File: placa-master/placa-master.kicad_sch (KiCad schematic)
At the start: 3 parts, among them J10 Enlace_placas, U4 MCP23017-E/SO

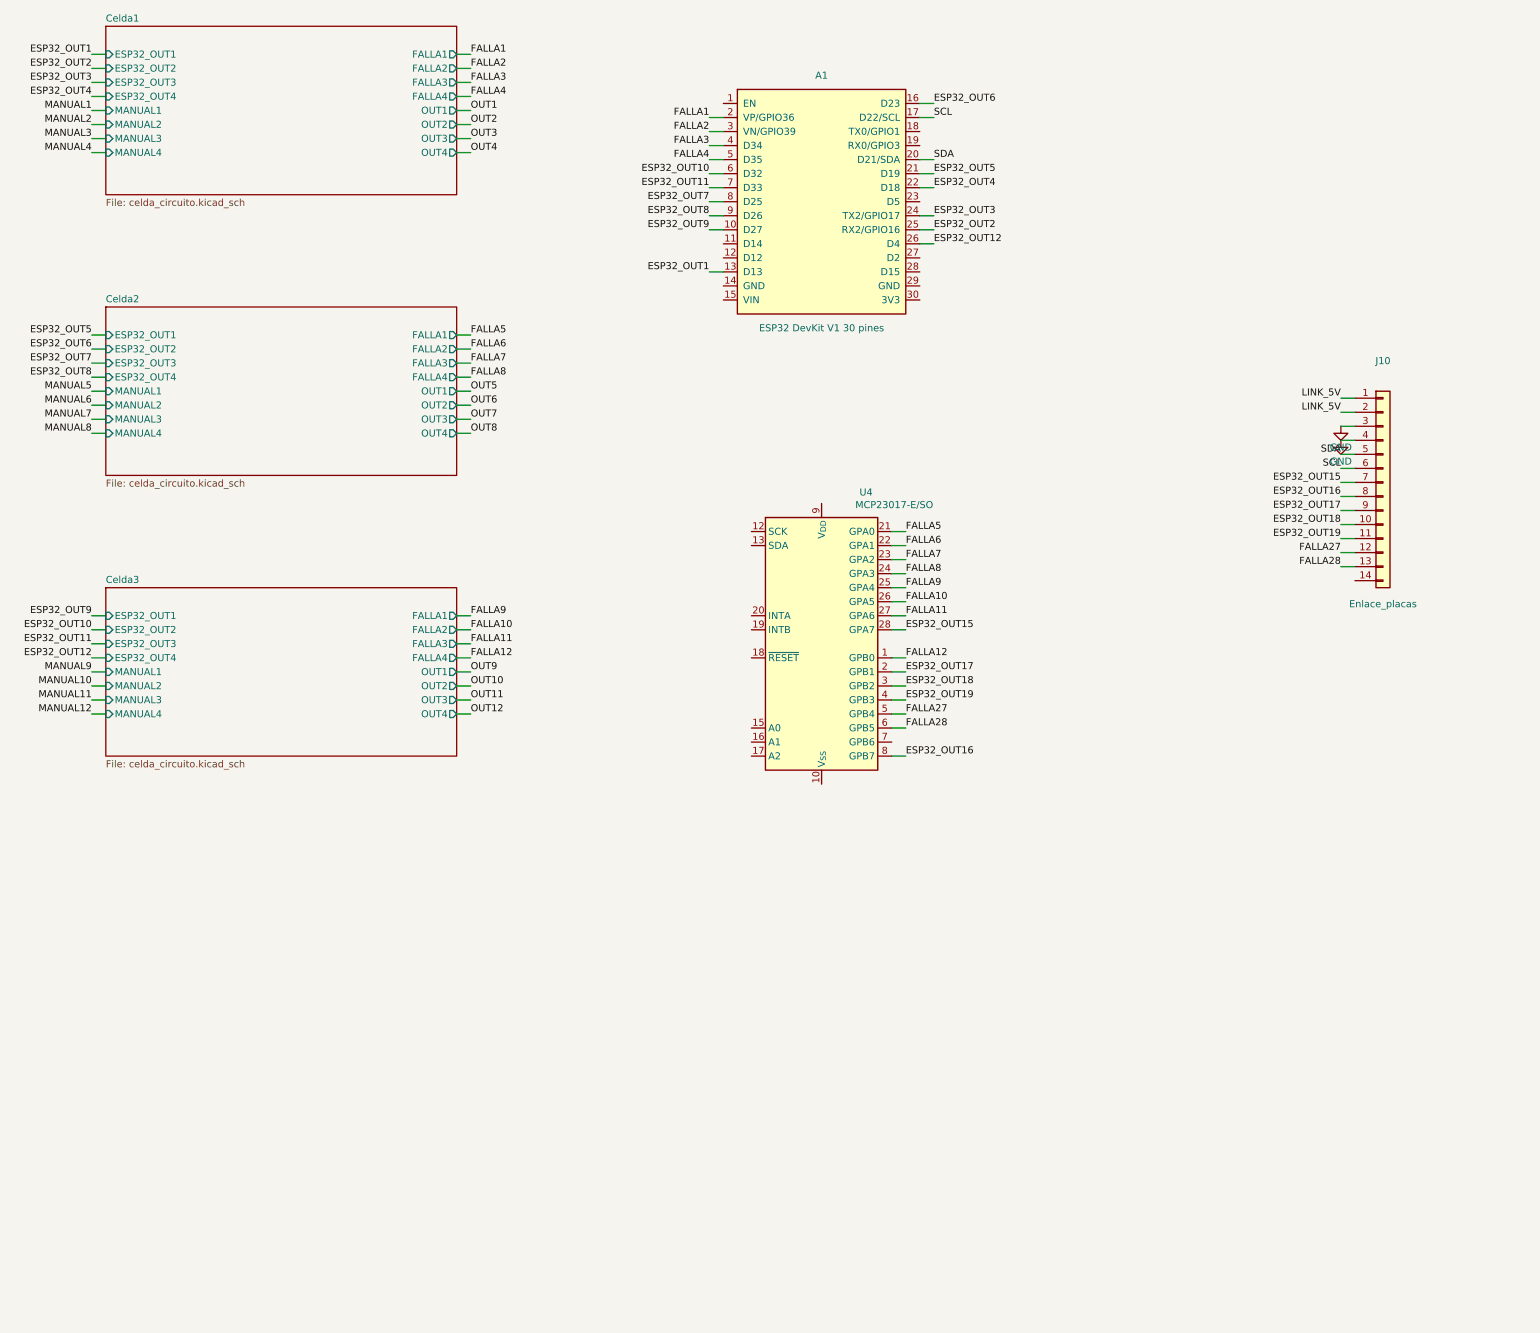
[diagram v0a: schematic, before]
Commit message: Cablea alimentación e I2C de las placas y replica las celdas en los PCB
Esquemáticos raíz: se cablean VDD, VSS, RESET, direcciones y SDA/SCL de los
MCP, los pull-ups de I2C (solo en la master), el LDO de 3,3 V y la entrada de
+12 V de la master, y la unión de las redes del bloque de poder en la slave.

PCB: nuevo herramientas/replicar_celdas_pcb.py que copia la celda dorada por
traslación en cada placa (master en una fila de 3 celdas, slave en 2 x 2), con
pistas, vías, serigrafía y planos GND/+3,3 V. Coloca además las huellas de la
raíz (ESP32, MCP, bloque de poder, conector) en una franja provisional bajo
las celdas, ya enlazadas al esquemático. Sin tiras de +12 V a propósito: se
dibujan al final. La master incluye los ajustes manuales hechos en KiCad.
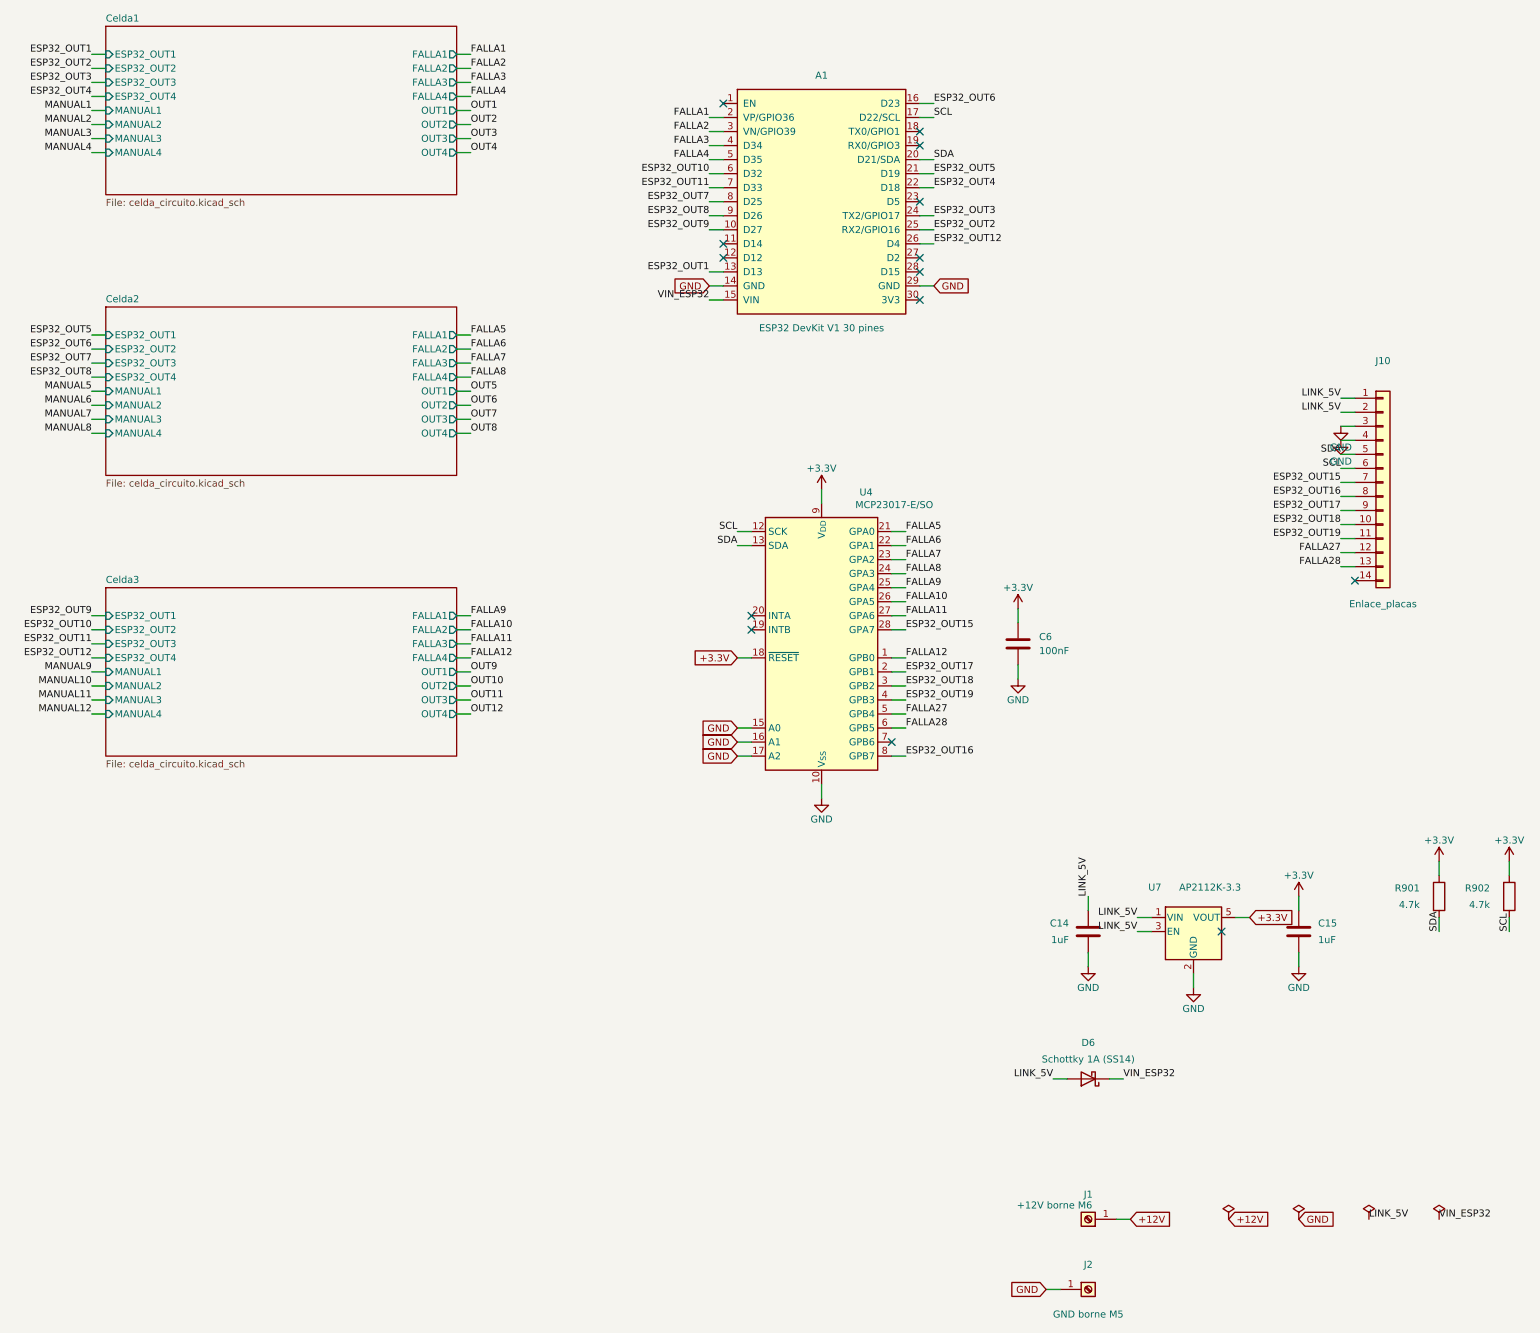
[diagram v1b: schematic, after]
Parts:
- added C14, C15: 1uF, Capacitor_SMD:C_0805_2012Metric, symbol Device:C
- added C6: 100nF, Capacitor_SMD:C_0805_2012Metric, symbol Device:C
- added D6: Schottky 1A (SS14), Diode_SMD:D_SMA, symbol Device:D_Schottky
- added J1: +12V borne M6, MountingHole:MountingHole_6.4mm_M6_Pad, symbol Connector:Screw_Terminal_01x01
- added J2: GND borne M5, MountingHole:MountingHole_5.3mm_M5_Pad, symbol Connector:Screw_Terminal_01x01
- added R901, R902: 4.7k, Resistor_SMD:R_0805_2012Metric, symbol Device:R
- added U7: AP2112K-3.3, Package_TO_SOT_SMD:SOT-23-5, symbol Regulator_Linear:AP2112K-3.3
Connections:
- net GND: now also A1.14 (GND), A1.29 (GND), U4.10 (V_{SS}), U4.15 (A0), U4.16 (A1), U4.17 (A2), C14.2, C15.2, C6.2, J2.1 (Pin_1), U7.2 (GND)
- net LINK_5V: now also C14.1, D6.2 (A), U7.1 (VIN), U7.3 (EN)
- net SCL: now also U4.12 (SCK), R902.2
- net SDA: now also U4.13 (SDA), R901.2
- net VIN_ESP32: now reaches A1.15 (VIN)
- net VIN_ESP32: now also D6.1 (K)
- net +3.3V: now reaches U4.18 (~{RESET})
- net +3.3V: now also U4.9 (V_{DD}), C15.1, C6.1, R901.1, R902.1, U7.5 (VOUT)
- new net +12V: J1.1 (Pin_1)
- no-connect marks 0 -> 14
